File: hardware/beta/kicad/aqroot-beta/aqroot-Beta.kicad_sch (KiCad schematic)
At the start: 0 parts

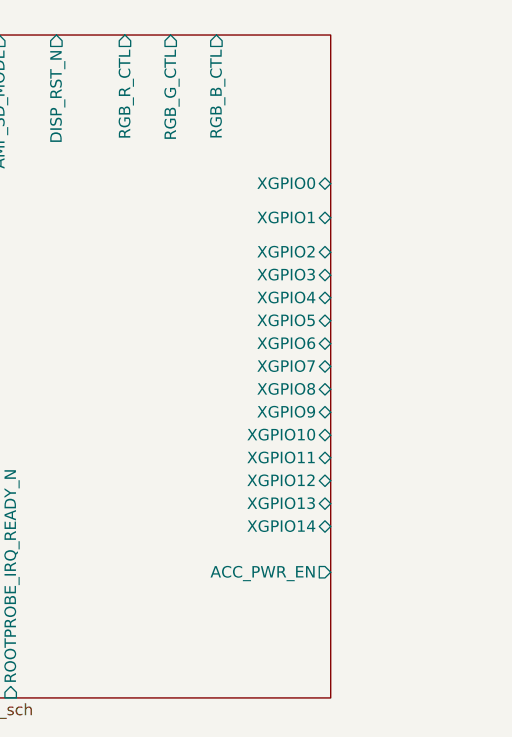
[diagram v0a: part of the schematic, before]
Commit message: AQROOT Beta: complete community-header hierarchy integration
Connects XGPIO0-14 between U3 (TCA9535 port expander, sheet 08) and the
100R series resistors R51-R65 on sheet 09, replacing the 15 sheet-local
/08_BUTTONS_EXPANDERS/XGPIOx fragments with root-level /XGPIOx nets.

Connects ACC_PWR_EN between U3 pin 20 (P17) and the accessory rail
control: U15 pin 3 (TPS22918 ON) and U16 pin 5 (TCA9517A EN), joining
the existing R17 100k pull-down on one root-level /ACC_PWR_EN net. The
accessory load switch and I2C buffer enable are now actually driven by
U3 rather than floating.

Adds the missing FAST_IO boot-log warning note to sheet 09: FAST_IO is
U0TXD and emits the UART boot log at reset, so it must not be connected
to power enables or high-current loads.

Root-level hierarchy wiring only, except for the documentation text.
No component, value, footprint or pin-map changes: the component set is
unchanged at 158 parts and the J5 pin map, XGPIO series/ESD circuitry,
WAKE circuitry and FAST_IO electrical circuitry are untouched. No child
sheet required a schematic change.

ERC improves from 229 to 167 violations. This is not ERC-clean and not
fabrication-ready.

Co-Authored-By: Claude Opus 5 <noreply@anthropic.com>
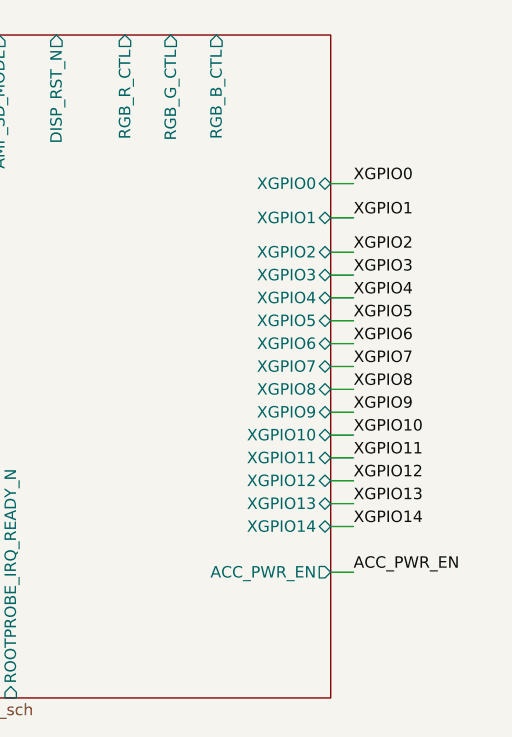
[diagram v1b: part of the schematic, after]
